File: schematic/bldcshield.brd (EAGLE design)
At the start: 51 parts, among them IC3 IR2101SMD, IC4 IR2101SMD, IC5 IR2101SMD

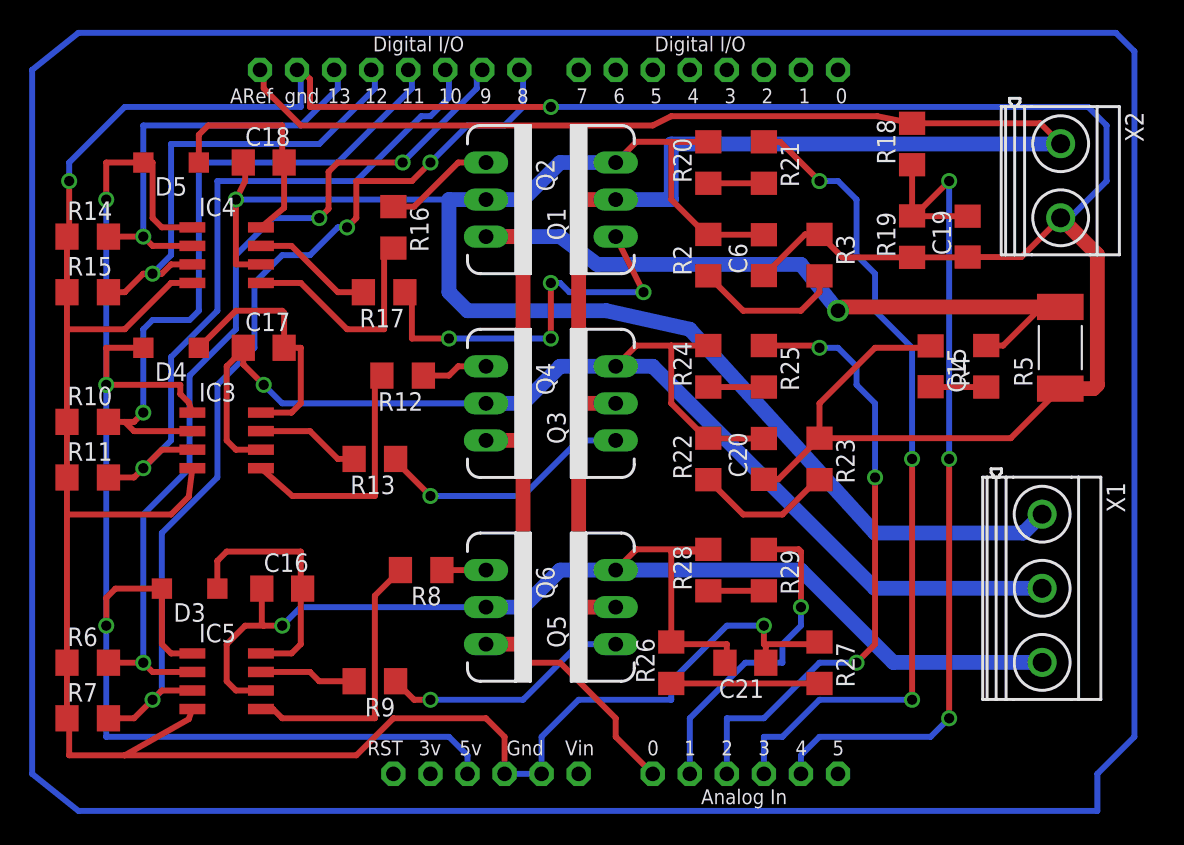
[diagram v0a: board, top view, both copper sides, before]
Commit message: Gerbers and some board changes
Need to edit the shield part because the board is off when rendered.
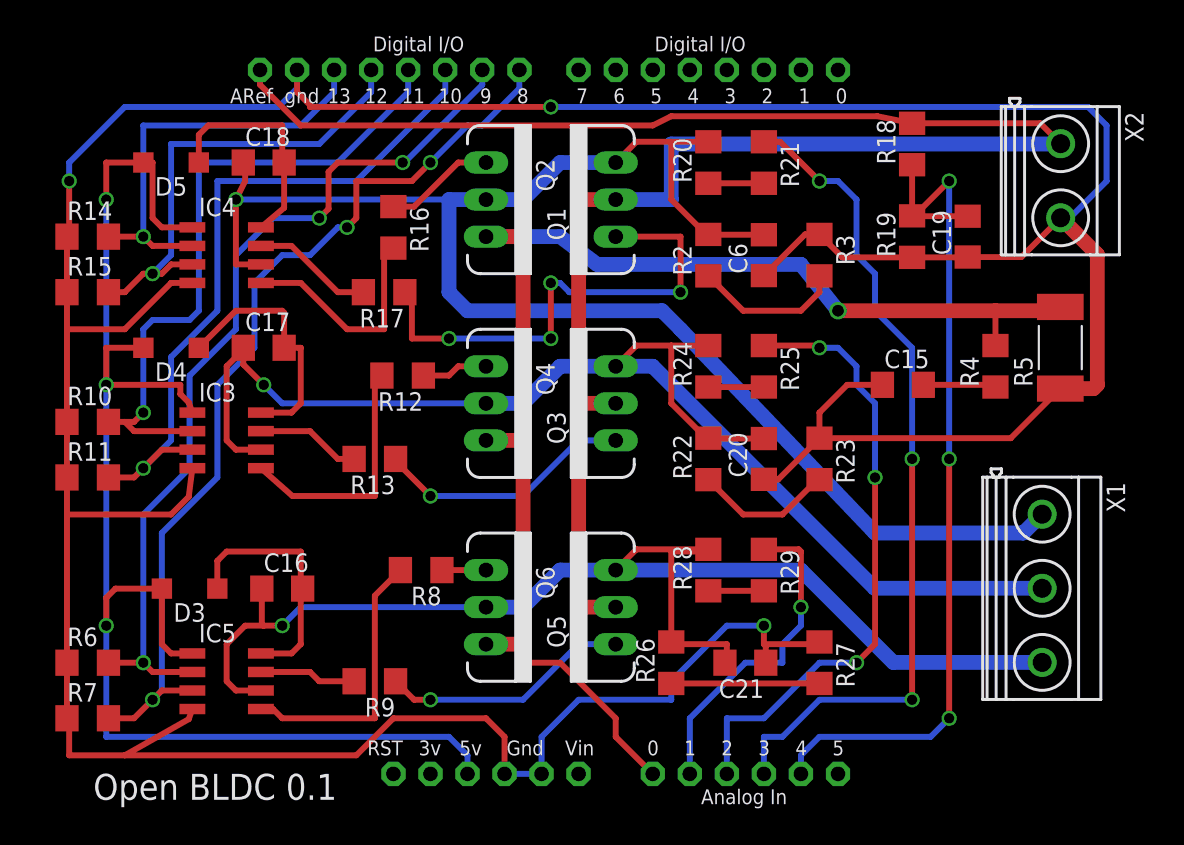
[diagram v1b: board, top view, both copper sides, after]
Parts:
- moved C15 2.29 mm to (80.6, 43.2), turned to 0 degrees
- moved R4 0.64 mm to (87.0, 44.5)
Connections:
- new net LO_2: E$1.D11
- new net S$4: R4.2
- new net S$8: E$1.D9
- net CURRENT: no longer R4.2, R5.2
- net HI_1: now also E$1.D12
- net HI_3: now also E$1.D8
- net LO_1: now also E$1.D13
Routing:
- net S$1: track 252.3 -> 0.00 mm
- net S$3: track 138.9 -> 127.4 mm
- net LO_3: track 60.9 -> 52.1 mm
- net S$8: track 0.00 -> 8.56 mm
- net N$30: track 27.6 -> 34.1 mm
- net S$7: track 0.00 -> 6.50 mm
- net S$6: track 0.00 -> 5.08 mm
- net N$9: track 3.82 -> 0.00 mm
- net CURRENT: track 96.2 -> 92.4 mm
- net BLDC3: track 90.6 -> 89.3 mm
- net S$2: track 151.9 -> 150.9 mm
- net HI_3: track 65.5 -> 64.5 mm
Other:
- board text added: "Open BLDC 0.1"
- board text added: "www.OpenRover.com"

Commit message: redoing brf layout from scatch
deleted gerbers and backed up brd file
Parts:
- removed C15, C19: 22p, SmartPrj:C1206
- removed C16, C17, C18: 100nf, SmartPrj:C1206
- removed C20, C21: 100pF, SmartPrj:C1206
- removed D4, D5: MMSD914, diode:SOD123
- removed E$1: (no value), adafruit:ARDUINO-NOHOLE
- removed IC4, IC5: IR2101SMD, IR:SO08
- removed R29: 15k, SmartPrj:R1206
- added C1, C4, C5: 100nf, SmartPrj:C1206
- added C2, C8: 22p, SmartPrj:C1206
- added C3, C7: 100pF, SmartPrj:C1206
- added D1, D2: MMSD914, diode:SOD123
- added IC1, IC2: IR2101SMD, IR:SO08
- added Q7: (no value), SparkFun:TO220V
- added R1: 200K, SmartPrj:R1206
- Q3: value (none) -> Shield; device SparkFun:TO220V -> adafruit:ARDUINOR3-BLDC
- R10: value 10k -> 22k
- R11, R14, R6: value 10k -> 22
- R12, R13: value 22 -> 10k
- R15, R7: value 10k -> 100k
- R16, R8: value 22 -> 15k
- R17, R9: value 22 -> 22k
- R18: value 200K -> 22k
- R19: value 68k -> 22
- R2: value 22k -> 68k
- R20: value 100k -> 10k
- R21: value 15k -> 10k
- R22, R3: value 22k -> 22
- R23: value 22k -> 100k
- R24: value 100k -> 15k
- R25: value 15k -> 22k
- R27: value 22k -> 4.7k
- R28: value 100k -> 0.001; device SmartPrj:R1206 -> resistor:R2512
- R4: value 4.7k -> 10k
- R5: value 0.001 -> 10k; device resistor:R2512 -> SmartPrj:R1206
- X1: device con-phoenix-508:MKDSN1,5/3-5,08 -> con-phoenix-508:MKDSN1,5/2-5,08
- X2: device con-phoenix-508:MKDSN1,5/2-5,08 -> con-phoenix-508:MKDSN1,5/3-5,08
- moved R7 83.7 mm to (90.6, 72.1), turned to 180 degrees
- moved R15 66.3 mm to (90.5, 58.0), turned to 180 degrees
- moved R9 62.8 mm to (83.6, 72.0), turned to 0 degrees
- moved R10 62.8 mm to (82.0, 66.5), turned to 90 degrees
- moved R5 59.8 mm to (34.5, 64.0), turned to 0 degrees
- moved R4 57.5 mm to (34.5, 68.0), turned to 0 degrees
- moved R8 55.7 mm to (90.1, 66.5), turned to 90 degrees
- moved R6 52.9 mm to (59.5, 64.0), turned to 180 degrees
- moved R28 49.5 mm to (107.1, 59.9), turned to 270 degrees
- moved X1 47.9 mm to (108.8, 70.8)
- moved R16 44.3 mm to (90.0, 52.6), turned to 90 degrees
- moved R2 42.2 mm to (105.8, 34.8), turned to 180 degrees
- moved R21 42.1 mm to (35.6, 36.0), turned to 0 degrees
- moved R27 40.0 mm to (101.0, 54.4)
- moved R17 39.5 mm to (83.7, 58.1), turned to 0 degrees
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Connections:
- removed net S$2: C21.1, IC3.4, IC4.4, IC5.4, R10.1, R11.1, R14.1, R15.1, R27.1, R6.1, R7.1
- removed net S$3: C15.1, C19.1, C20.1, C6.1, R19.1, R23.1, R3.1, R5.1, X2.2
- removed net S$4: R4.2
- removed net S$5: IC3.2
- removed net S$8: E$1.D9
- new net +3V3: Q3.3V
- new net GND: C2.1, C3.1, C6.1, C7.1, C8.1, IC1.4, IC2.4, IC3.4, Q3.GND, Q3.GND1, Q3.GND2, R10.1, R12.1, R13.1, R18.1, R2.1, R20.1, R21.1, R26.1, R28.1, R4.1, R5.1, X1.2
- net +5V: now also D1.A, D2.A, IC1.1, IC2.1, Q3.5V, Q3.VIN; no longer D4.A, D5.A, IC4.1, IC5.1
- net BLDC1: now also C1.1, C3.2, IC1.6, R7.2, R9.2, X2.1; no longer C18.1, C6.2, IC4.6, R2.2, R20.2, X1.1
- net BLDC2: now also C4.1, C6.2, IC2.6, Q4.3, Q5.2, R15.2, R17.2, X2.2; no longer C17.1, C20.2, IC3.6, Q3.3, Q4.2, R22.2, R24.2, X1.2
- net BLDC3: now also C5.1, C7.2, IC3.6, Q6.3, Q7.2, R23.2, R25.2, X2.3; no longer C16.1, C21.2, IC5.6, Q5.3, Q6.2, R26.2, R28.2, X1.3
- net CURRENT: now also Q3.A0, Q5.3, Q7.3, R27.2, R28.2; no longer Q4.3, Q6.3
- net EMF1: now also Q3.A3, R8.1; no longer R21.1
- net EMF2: now also Q3.A2, R16.1; no longer R25.1
- net EMF3: now also Q3.A1, R24.1; no longer R29.1
- net HI_1: now also IC1.3, Q3.D12, R5.2; no longer E$1.D12, IC4.3, R15.2
- net HI_2: now also IC2.3, Q3.D10, R13.2; no longer IC3.3, R11.2
- net HI_3: now also IC3.3, Q3.D8, R21.2; no longer E$1.D8, IC5.3, R7.2
- net LOW_VOLTAGE: now also C2.2, Q3.A4, R1.1, R2.2; no longer C19.2, R18.1, R19.2
- net LO_1: now also IC1.2, Q3.D13, R4.2; no longer E$1.D13, IC4.2, R14.2
- net LO_2: now also IC2.2, Q3.D11, R12.2; no longer E$1.D11
- net LO_3: now also IC3.2, Q3.D9, R20.2; no longer IC5.2, R6.2
- net N$1: now also Q4.1, R11.1; no longer Q3.1, R13.1
- net N$10: now also R7.1, R8.2; no longer R20.1, R21.2
- net N$12: now also R17.1, R18.2; no longer R22.1, R23.2
- net N$13: now also IC3.7, R19.2; no longer IC5.7, R9.2
- net N$14: now also Q6.1, R19.1; no longer Q5.1, R9.1
- net N$15: now also Q7.1, R22.1; no longer Q6.1, R8.1
- net N$16: now also IC3.5, R22.2; no longer IC5.5, R8.2
- net N$17: now also C5.2, IC3.8; no longer C16.2, IC5.8
- net N$19: now also R15.1, R16.2; no longer R24.1, R25.2
- net N$2: now also R10.2, R9.1; no longer R2.1, R3.2
- net N$21: now also IC2.7, R11.2; no longer IC3.7, R13.2
- net N$23: now also Q5.1, R14.1; no longer Q4.1, R12.1
- net N$24: now also IC2.5, R14.2; no longer IC3.5, R12.2
- net N$25: now also C4.2, D2.C, IC2.8; no longer C17.2, D4.C, IC3.8
- net N$26: now also R25.1, R26.2; no longer R26.1, R27.2
- net N$28: now also R23.1, R24.2; no longer R28.1, R29.2
- net N$29: now also IC1.7, R3.2; no longer IC4.7, R17.2
- net N$30: now also R3.1; no longer R17.1
- net N$31: now also R6.1; no longer R16.1
- net N$32: now also IC1.5, R6.2; no longer IC4.5, R16.2
- net N$33: now also C1.2, D1.C, IC1.8; no longer C18.2, D5.C, IC4.8
- net N$9: now also C8.2, R27.1; no longer C15.2, R4.1
- net VCC: now also Q3.AREF, Q4.2, Q6.2, R1.2, X1.1; no longer Q3.2, Q5.2, R18.2, X2.1
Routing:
- net S$2: track 150.9 -> 0.00 mm, vias 1 -> 0
- net GND: track 0.00 -> 141.0 mm, vias 0 -> 3
- net S$3: track 127.4 -> 0.00 mm, vias 1 -> 0
- net +5V: track 100.4 -> 0.00 mm, vias 3 -> 0
- net HI_3: track 64.5 -> 0.00 mm, vias 3 -> 0
- net LO_3: track 52.1 -> 0.00 mm, vias 3 -> 0
- net HI_2: track 48.0 -> 0.00 mm
- net LO_2: track 45.0 -> 0.00 mm, vias 1 -> 0
- net LOW_VOLTAGE: track 60.2 -> 23.8 mm, vias 3 -> 0
- net N$30: track 34.1 -> 0.00 mm, vias 4 -> 0
- net HI_1: track 31.4 -> 0.00 mm, vias 1 -> 0
- net LO_1: track 28.7 -> 0.00 mm, vias 1 -> 0
- net CURRENT: track 92.4 -> 113.2 mm
- net N$16: track 19.0 -> 0.00 mm
- net BLDC1: track 108.9 -> 90.5 mm, vias 1 -> 0
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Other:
- board outline added: 160 x 100 mm
- board text removed: "Open BLDC 0.1"
- board text removed: "www.OpenRover.com"
